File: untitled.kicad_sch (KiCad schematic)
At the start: 13 parts, among them Q1 IRFB7730PBF, Q2 IRFB7730PBF, U1 IR2109, U2 LM317_TO-220

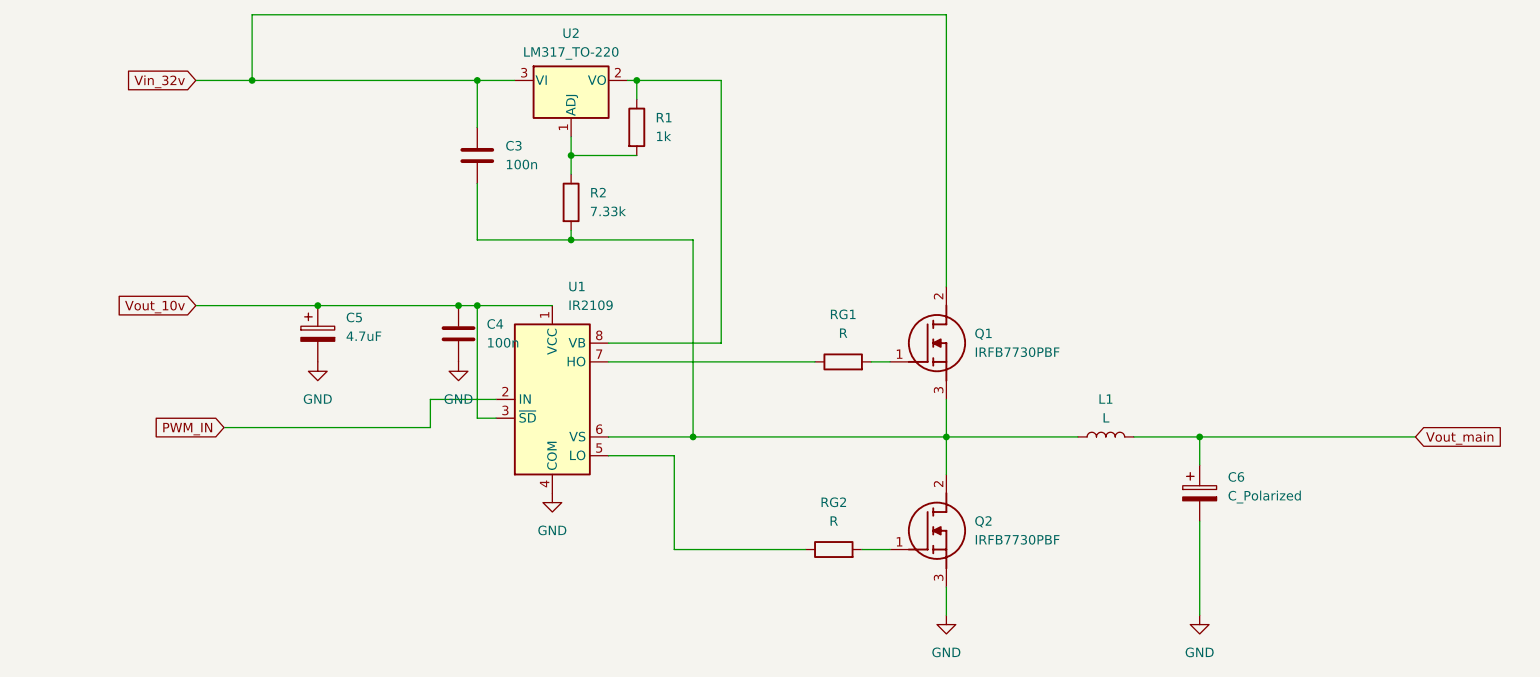
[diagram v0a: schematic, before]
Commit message: dodanie zasilania pomocniczego 10v oraz 5v i
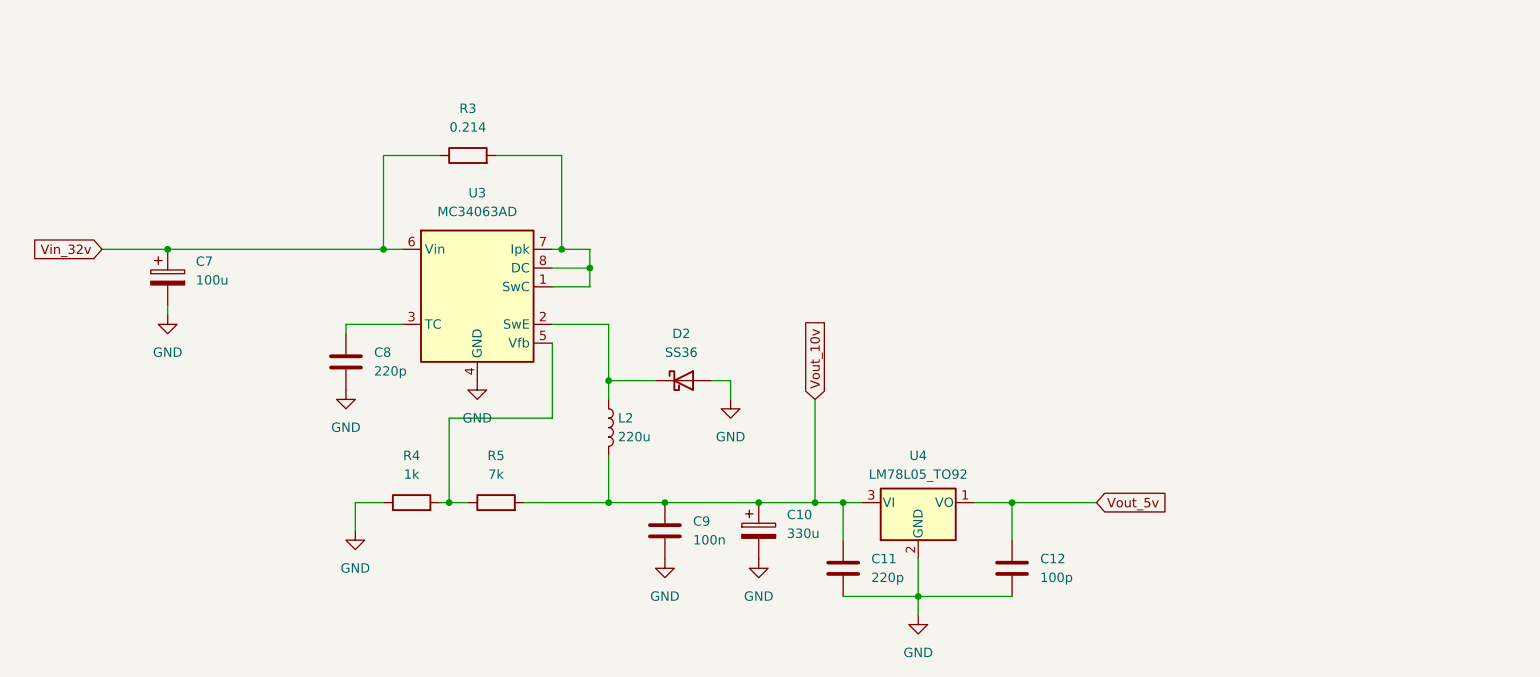
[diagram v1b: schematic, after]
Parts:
- removed C3, C4: 100n, symbol Device:C
- removed C5: 4.7uF, symbol Device:C_Polarized
- removed C6: C_Polarized, symbol Device:C_Polarized
- removed L1: L, symbol Device:L
- removed Q1, Q2: IRFB7730PBF, TO254P483X1016X1994-3P, symbol IRFB7730PBF:IRFB7730PBF
- removed R1: 1k, symbol Device:R
- removed R2: 7.33k, symbol Device:R
- removed RG1, RG2: R, symbol Device:R
- removed U1: IR2109, symbol Driver_FET:IR2109
- removed U2: LM317_TO-220, Package_TO_SOT_THT:TO-220-3_Vertical, symbol Regulator_Linear:LM317_TO-220
- added C10: 330u, symbol Device:C_Polarized
- added C11, C8: 220p, symbol Device:C
- added C12: 100p, symbol Device:C
- added C7: 100u, symbol Device:C_Polarized
- added C9: 100n, symbol Device:C
- added D2: SS36, Diode_SMD:D_SMA, symbol Diode:SS36
- added L2: 220u, symbol Device:L
- added R3: 0.214, symbol Device:R
- added R4: 1k, symbol Device:R
- added R5: 7k, symbol Device:R
- added U3: MC34063AD, Package_SO:SOIC-8_3.9x4.9mm_P1.27mm, symbol Regulator_Switching:MC34063AD
- added U4: LM78L05_TO92, Package_TO_SOT_THT:TO-92_Inline, symbol Regulator_Linear:LM78L05_TO92
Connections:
- net GND: now also C10.2, C11.2, C12.2, C7.2, C8.2, C9.2, D2.2 (A), R4.1, U3.4 (GND), U4.2 (GND)
- net Vin_32v: now also C7.1, R3.1, U3.6 (Vin)
- net Vout_10v: now also C10.1, C11.1, C9.1, L2.2, R5.2, U4.3 (VI)
- new net: R4.2, R5.1, U3.5 (Vfb)
- new net: R3.2, U3.1 (SwC), U3.7 (Ipk), U3.8 (DC)
- new net: D2.1 (K), L2.1, U3.2 (SwE)
- new net: C8.1, U3.3 (TC)
- new net Vout_5v: C12.1, U4.1 (VO)
